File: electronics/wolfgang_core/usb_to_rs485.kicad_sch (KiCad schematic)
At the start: 10 parts

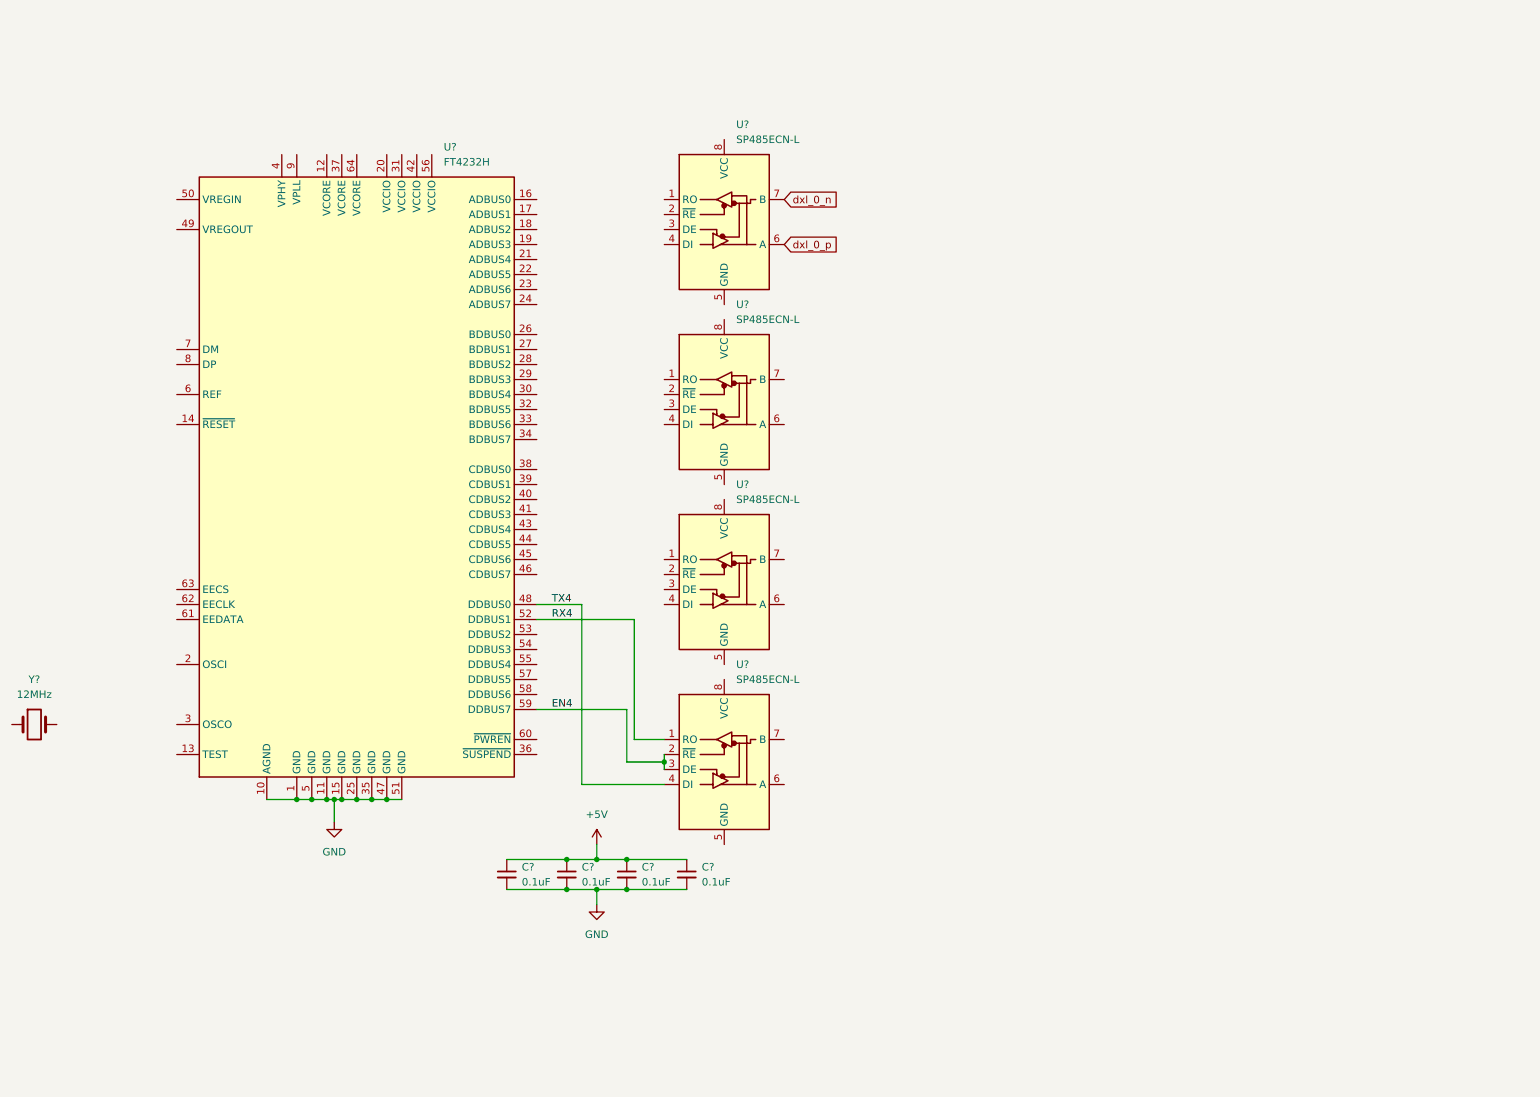
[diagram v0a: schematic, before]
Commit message: Initial version USB to RS485
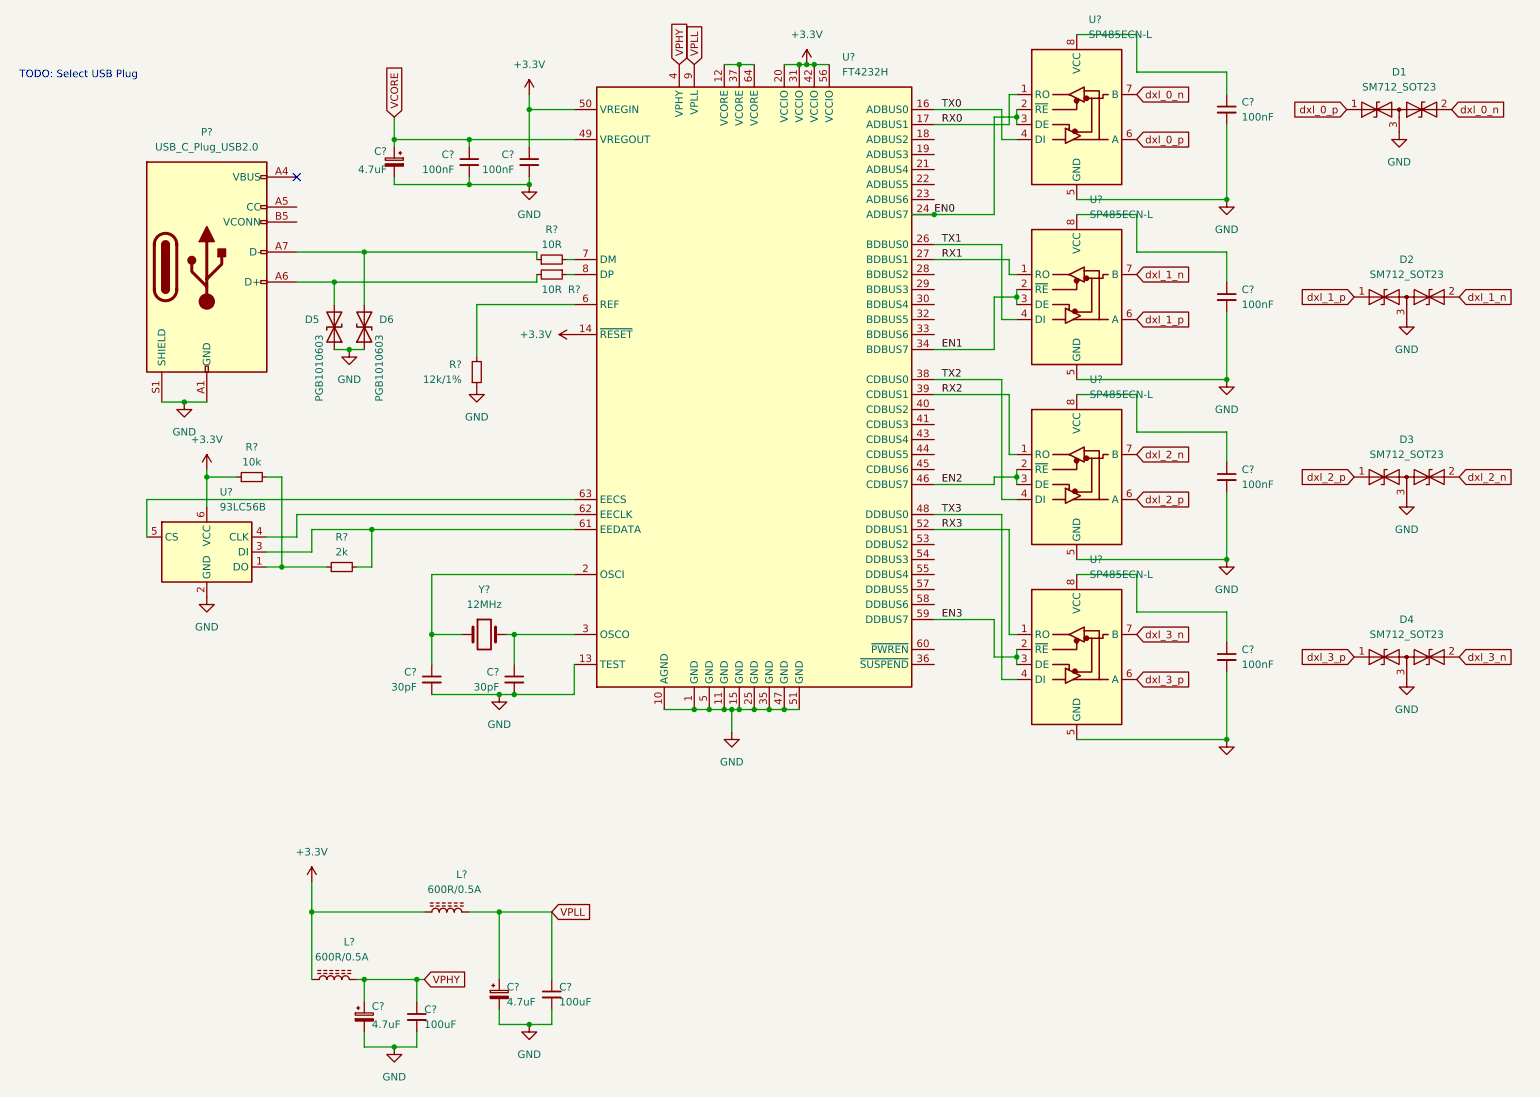
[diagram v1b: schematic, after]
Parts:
- removed C? (x4): 0.1uF, symbol Device:C_Small
- added C? (x2): 30pF, symbol Device:C_Small
- added C? (x2): 100uF, symbol Device:C_Small
- added C? (x6): 100nF, symbol Device:C_Small
- added C? (x3): 4.7uF, symbol Device:C_Polarized_Small
- added D1, D2, D3, D4: SM712_SOT23, Package_TO_SOT_SMD:SOT-23, symbol Diode:SM712_SOT23
- added D5, D6: PGB1010603, symbol Device:D_TVS
- added L? (x2): 600R/0.5A, symbol Device:L_Ferrite
- added P?: USB_C_Plug_USB2.0, symbol Connector:USB_C_Plug_USB2.0
- added R? (x2): 10R, symbol Device:R_Small
- added R?: 2k, symbol Device:R_Small
- added R?: 12k/1%, symbol Device:R_Small
- added R?: 10k, symbol Device:R_Small
- added U?: 93LC56B, Package_TO_SOT_SMD:SOT-23-6, symbol Memory_EEPROM:93LCxxBxxOT
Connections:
- net GND: now also U?.13 (TEST), U?.5 (GND), U?.5 (GND), U?.5 (GND), U?.5 (GND), C?.2, C?.2, C?.2, C?.2, C?.2, C?.2, C?.2, C?.2, C?.2, C?.2, C?.2, C?.2, C?.2, D1.3 (common), D2.3 (common), D3.3 (common), D4.3 (common), D5.1 (A1), D6.1 (A1), P?.A1 (GND), P?.A12 (GND), P?.B1 (GND), P?.B12 (GND), P?.S1 (SHIELD), R?.1, U?.2 (GND)
- net dxl_0_n: now also D1.2 (A2)
- net dxl_0_p: now also D1.1 (A1)
- net RX2: now reaches U?.1 (RO)
- net RX2: now also U?.39 (CDBUS1)
- net EN2: now reaches U?.2 (~{RE})
- net EN2: now also U?.3 (DE), U?.46 (CDBUS7)
- net TX2: now reaches U?.4 (DI)
- net TX2: now also U?.38 (CDBUS0)
- net dxl_2_p: now reaches U?.6 (A)
- net dxl_2_p: now also D3.1 (A1)
- net dxl_2_n: now reaches U?.7 (B)
- net dxl_2_n: now also D3.2 (A2)
- net at U?.8 (VCC): now also C?.1 (x4)
- net RX0: now reaches U?.1 (RO)
- net RX0: now also U?.17 (ADBUS1)
- net EN0: now reaches U?.2 (~{RE})
- net EN0: now also U?.24 (ADBUS7), U?.3 (DE)
- net TX0: now reaches U?.4 (DI)
- net TX0: now also U?.16 (ADBUS0)
- net at Y?.1: now also U?.2 (OSCI), C?.1
- net at Y?.2: now also U?.3 (OSCO), C?.1
- net dxl_3_p: now reaches U?.6 (A)
- net dxl_3_p: now also D4.1 (A1)
- net dxl_3_n: now reaches U?.7 (B)
- net dxl_3_n: now also D4.2 (A2)
- net at U?.12 (VCORE): now also U?.37 (VCORE), U?.64 (VCORE)
- net +3.3V: now reaches U?.14 (~{RESET})
- net +3.3V: now also U?.20 (VCCIO), U?.31 (VCCIO), U?.42 (VCCIO), U?.50 (VREGIN), U?.56 (VCCIO), C?.1, L?.1, L?.1, R?.1, U?.6 (VCC)
- net TX1: now reaches U?.26 (BDBUS0)
- net TX1: now also U?.4 (DI)
- net RX1: now reaches U?.27 (BDBUS1)
- net RX1: now also U?.1 (RO)
- net EN1: now reaches U?.34 (BDBUS7)
- net EN1: now also U?.2 (~{RE}), U?.3 (DE)
- net VPHY: now reaches U?.4 (VPHY)
- net VPHY: now also C?.1, C?.1, L?.2
- net VCORE: now reaches U?.49 (VREGOUT)
- net VCORE: now also C?.1, C?.1
- net at U?.6 (REF): now also R?.2
- net at U?.61 (EEDATA): now also R?.2, U?.3 (DI)
- net at U?.62 (EECLK): now also U?.4 (CLK)
- net at U?.63 (EECS): now also U?.5 (CS)
- net at U?.7 (DM): now also R?.2
- net at U?.8 (DP): now also R?.1
- net VPLL: now reaches U?.9 (VPLL)
- net VPLL: now also C?.1, C?.1, L?.2
- net dxl_1_p: now reaches U?.6 (A)
- net dxl_1_p: now also D2.1 (A1)
- net dxl_1_n: now reaches U?.7 (B)
- net dxl_1_n: now also D2.2 (A2)
- net EN4 renamed EN3
- net RX4 renamed RX3
- net TX4 renamed TX3
- new net: D5.2 (A2), P?.A6 (D+), R?.2
- new net: P?.A4 (VBUS), P?.A9 (VBUS), P?.B4 (VBUS), P?.B9 (VBUS)
- new net: D6.2 (A2), P?.A7 (D-), R?.1
- new net: R?.1, R?.2, U?.1 (DO)
- no-connect marks 0 -> 1
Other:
- note added: "TODO: Select USB Plug"
- moved on the sheet: U?, Y?
